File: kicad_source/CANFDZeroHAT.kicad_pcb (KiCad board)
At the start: 2 copper layers, 65 x 30 mm, 33 parts, among them CN1 RASPI-IO, CN2 691322310004, CN3 GH_SM04B-GHS-TB, CN4 GH_SM04B-GHS-TB, SW1 JS202011JCQN, U1 MCP2518FD, U2 TCAN332GDR, Y1 RH100-40.000-18-F-2050-TR

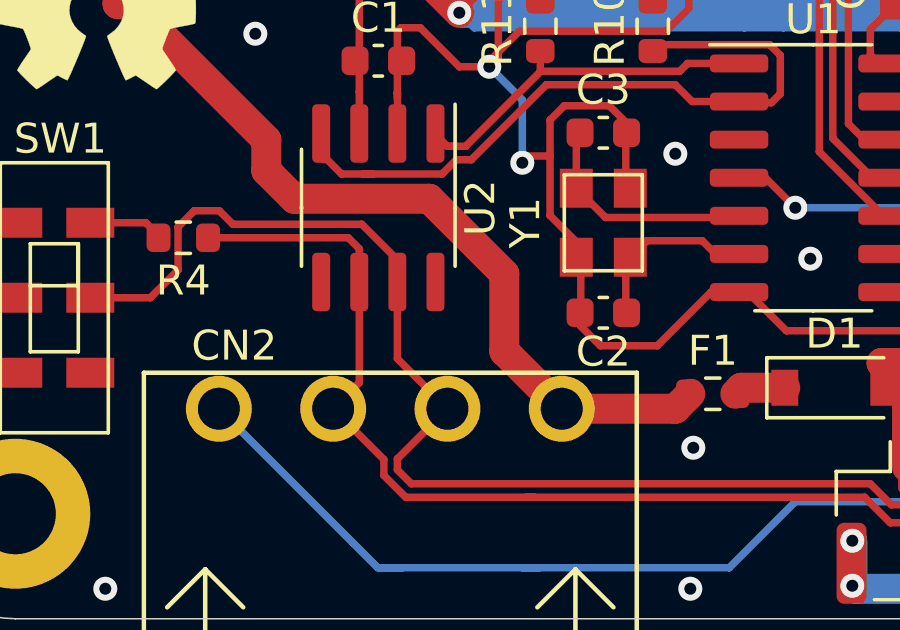
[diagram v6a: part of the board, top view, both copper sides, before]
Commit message: updated symbol of CAN driver
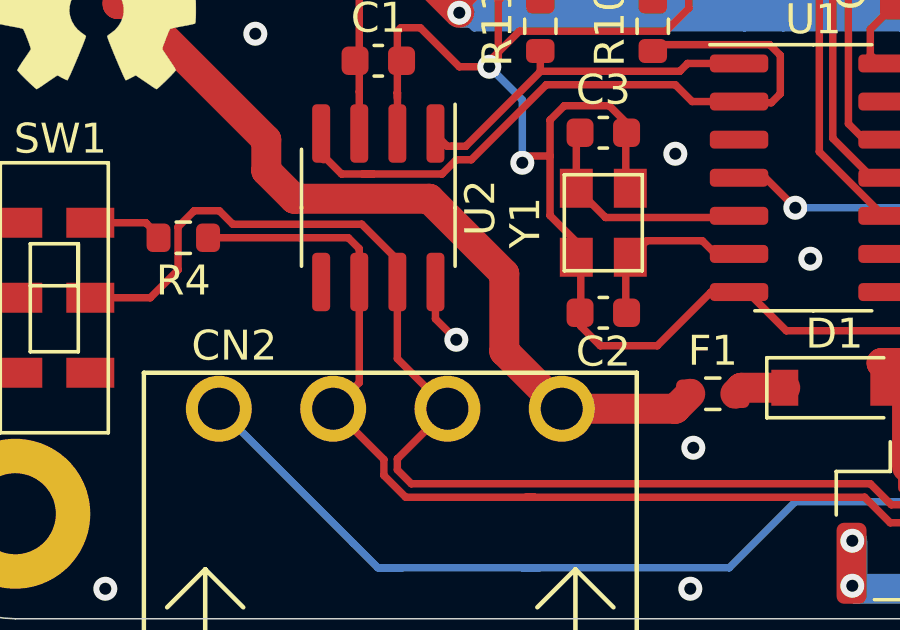
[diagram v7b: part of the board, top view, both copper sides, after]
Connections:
- U2 pad 8: unconnected-(U2-Pad8) -> GND
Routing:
- net GND: track 195.9 -> 198.1 mm, vias 22 -> 23
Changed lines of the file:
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@@
   (net 49 "unconnected-(U1-Pad9)")
   (net 50 "unconnected-(U2-Pad5)")
-  (net 51 "unconnected-(U2-Pad8)")
-  (net 52 "/MP")
-  (net 53 "unconnected-(SW1-Pad4)")
-  (net 54 "unconnected-(SW1-Pad5)")
-  (net 55 "unconnected-(SW1-Pad6)")
+  (net 51 "/MP")
+  (net 52 "unconnected-(SW1-Pad4)")
+  (net 53 "unconnected-(SW1-Pad5)")
+  (net 54 "unconnected-(SW1-Pad6)")
   (footprint "Capacitor_SMD:C_0603_1608Metric" (layer "F.Cu")
     (at 123.1 97.9)
@@
       (net 3 "GND") (pinfunction "Pin_4") (pintype "passive"))
     (pad "MP" smd roundrect (at 3.725 1.35) (size 1 2.7) (layers "F.Cu" "F.Paste" "F.Mask") (roundrect_rratio 0.25)
-      (net 52 "/MP") (pinfunction "MountPin") (pintype "passive"))
+      (net 51 "/MP") (pinfunction "MountPin") (pintype "passive"))
     (pad "MP" smd roundrect (at -3.725 1.35) (size 1 2.7) (layers "F.Cu" "F.Paste" "F.Mask") (roundrect_rratio 0.25)
-      (net 52 "/MP") (pinfunction "MountPin") (pintype "passive"))
+      (net 51 "/MP") (pinfunction "MountPin") (pintype "passive"))
     (model "${KICAD6_3DMODEL_DIR}/Connector_JST.3dshapes/JST_GH_SM04B-GHS-TB_1x04-1MP_P1.25mm_Horizontal.wrl"
       (offset (xyz 0 0 0))
@@
       (net 3 "GND") (pinfunction "Pin_4") (pintype "passive"))
     (pad "MP" smd roundrect (at 3.725 1.35) (size 1 2.7) (layers "F.Cu" "F.Paste" "F.Mask") (roundrect_rratio 0.25)
-      (net 52 "/MP") (pinfunction "MountPin") (pintype "passive"))
+      (net 51 "/MP") (pinfunction "MountPin") (pintype "passive"))
     (pad "MP" smd roundrect (at -3.725 1.35) (size 1 2.7) (layers "F.Cu" "F.Paste" "F.Mask") (roundrect_rratio 0.25)
-      (net 52 "/MP") (pinfunction "MountPin") (pintype "passive"))
+      (net 51 "/MP") (pinfunction "MountPin") (pintype "passive"))
     (model "${KICAD6_3DMODEL_DIR}/Connector_JST.3dshapes/JST_GH_SM04B-GHS-TB_1x04-1MP_P1.25mm_Horizontal.wrl"
       (offset (xyz 0 0 0))
@@
       (net 46 "unconnected-(SW1-Pad3)") (pinfunction "C") (pintype "passive+no_connect"))
     (pad "4" smd rect locked (at -2.5 1.2 270) (size 1 1.6) (layers "F.Cu" "F.Paste" "F.Mask")
-      (net 53 "unconnected-(SW1-Pad4)") (pinfunction "A") (pintype "passive+no_connect"))
+      (net 52 "unconnected-(SW1-Pad4)") (pinfunction "A") (pintype "passive+no_connect"))
     (pad "5" smd rect locked (at 0 1.2 270) (size 1 1.6) (layers "F.Cu" "F.Paste" "F.Mask")
-      (net 54 "unconnected-(SW1-Pad5)") (pinfunction "B") (pintype "passive+no_connect"))
+      (net 53 "unconnected-(SW1-Pad5)") (pinfunction "B") (pintype "passive+no_connect"))
     (pad "6" smd rect locked (at 2.5 1.2 270) (size 1 1.6) (layers "F.Cu" "F.Paste" "F.Mask")
-      (net 55 "unconnected-(SW1-Pad6)") (pinfunction "C") (pintype "passive+no_connect"))
+      (net 54 "unconnected-(SW1-Pad6)") (pinfunction "C") (pintype "passive+no_connect"))
     (model "${KISYS3DMOD}/mechanical-switches.3dshapes/JS202011JCQN.stp"
       (offset (xyz 0 0 0))
@@
     (fp_line (start -1.95 -1.475) (end -0.975 -2.45) (layer "F.Fab") (width 0.1))
     (pad "1" smd roundrect (at -2.475 -1.905 270) (size 1.95 0.6) (layers "F.Cu" "F.Paste" "F.Mask") (roundrect_rratio 0.25)
-      (net 17 "/CAN_TX") (pinfunction "D") (pintype "output"))
+      (net 17 "/CAN_TX") (pinfunction "D") (pintype "input"))
     (pad "2" smd roundrect (at -2.475 -0.635 270) (size 1.95 0.6) (layers "F.Cu" "F.Paste" "F.Mask") (roundrect_rratio 0.25)
       (net 3 "GND") (pinfunction "GND") (pintype "power_in"))
@@
       (net 1 "+3.3V") (pinfunction "VCC") (pintype "power_in"))
     (pad "4" smd roundrect (at -2.475 1.905 270) (size 1.95 0.6) (layers "F.Cu" "F.Paste" "F.Mask") (roundrect_rratio 0.25)
-      (net 18 "/CAN_RX") (pinfunction "R") (pintype "input"))
+      (net 18 "/CAN_RX") (pinfunction "R") (pintype "output"))
     (pad "5" smd roundrect (at 2.475 1.905 270) (size 1.95 0.6) (layers "F.Cu" "F.Paste" "F.Mask") (roundrect_rratio 0.25)
-      (net 50 "unconnected-(U2-Pad5)") (pinfunction "NC2") (pintype "bidirectional+no_connect"))
+      (net 50 "unconnected-(U2-Pad5)") (pinfunction "Vref") (pintype "output+no_connect"))
     (pad "6" smd roundrect (at 2.475 0.635 270) (size 1.95 0.6) (layers "F.Cu" "F.Paste" "F.Mask") (roundrect_rratio 0.25)
       (net 13 "/CANL") (pinfunction "CANL") (pintype "bidirectional"))
@@
       (net 12 "/CANH") (pinfunction "CANH") (pintype "bidirectional"))
     (pad "8" smd roundrect (at 2.475 -1.905 270) (size 1.95 0.6) (layers "F.Cu" "F.Paste" "F.Mask") (roundrect_rratio 0.25)
-      (net 51 "unconnected-(U2-Pad8)") (pinfunction "NC1") (pintype "bidirectional+no_connect"))
+      (net 3 "GND") (pinfunction "Rs") (pintype "input"))
     (model "${KICAD6_3DMODEL_DIR}/Package_SO.3dshapes/SOIC-8_3.9x4.9mm_P1.27mm.wrl"
       (offset (xyz 0 0 0))
@@
   (segment (start 126.03 92.53) (end 126.163262 92.53) (width 0.25) (layer "F.Cu") (net 3))
   (segment (start 122.037001 89.817001) (end 124.577001 89.817001) (width 0.25) (layer "F.Cu") (net 3))
+  (segment (start 125.005 106.505) (end 125.7 107.2) (width 0.25) (layer "F.Cu") (net 3))
   (segment (start 127.1 97.8) (end 126.8 98.1) (width 0.25) (layer "F.Cu") (net 3))
   (segment (start 140.3 94.55) (end 141.55 94.55) (width 0.25) (layer "F.Cu") (net 3))
@@
   (segment (start 130.5 107.4) (end 132.4 107.4) (width 0.25) (layer "F.Cu") (net 3))
   (segment (start 123.7385 100.0955) (end 123.7385 98.9685) (width 0.25) (layer "F.Cu") (net 3))
+  (segment (start 125.005 105.275) (end 125.005 106.505) (width 0.25) (layer "F.Cu") (net 3))
   (segment (start 127.1 95.9) (end 127.1 97.8) (width 0.25) (layer "F.Cu") (net 3))
   (segment (start 151.35 106.9) (end 152.1 106.9) (width 0.25) (layer "F.Cu") (net 3))
@@
   (via (at 114 87.5) (size 0.8) (drill 0.4) (layers "F.Cu" "B.Cu") (net 3))
   (via (at 127.9 101.3) (size 0.8) (drill 0.4) (layers "F.Cu" "B.Cu") (net 3))
+  (via (at 125.7 107.2) (size 0.8) (drill 0.4) (layers "F.Cu" "B.Cu") (net 3))
   (via (at 171.5 93.5) (size 0.8) (drill 0.4) (layers "F.Cu" "B.Cu") (net 3))
   (via (at 144.6 114.4) (size 0.8) (drill 0.4) (layers "F.Cu" "B.Cu") (net 3))
@@
   (segment (start 128.5 94.7507) (end 128.2493 94.5) (width 0.25) (layer "F.Cu") (net 26))
   (segment (start 128.5 96) (end 128.5 94.7507) (width 0.25) (layer "F.Cu") (net 26))
-  (via (at 156.8 115.4) (size 0.8) (drill 0.4) (layers "F.Cu" "B.Cu") (net 52))
-  (via (at 146.3 115.4) (size 0.8) (drill 0.4) (layers "F.Cu" "B.Cu") (net 52))
-  (via (at 149.4 115.4) (size 0.8) (drill 0.4) (layers "F.Cu" "B.Cu") (net 52))
-  (via (at 146.3 113.9) (size 0.8) (drill 0.4) (layers "F.Cu" "B.Cu") (net 52))
-  (via (at 156.8 113.9) (size 0.8) (drill 0.4) (layers "F.Cu" "B.Cu") (net 52))
-  (via (at 149.4 113.9) (size 0.8) (drill 0.4) (layers "F.Cu" "B.Cu") (net 52))
-  (via (at 138.9 115.4) (size 0.8) (drill 0.4) (layers "F.Cu" "B.Cu") (net 52))
-  (via (at 138.9 113.9) (size 0.8) (drill 0.4) (layers "F.Cu" "B.Cu") (net 52))
-  (segment (start 138.9 115.4) (end 139 115.5) (width 1) (layer "B.Cu") (net 52))
-  (segment (start 146.3 113.9) (end 146.3 115.4) (width 1) (layer "B.Cu") (net 52))
-  (segment (start 146.3 115.4) (end 149.4 115.4) (width 1) (layer "B.Cu") (net 52))
-  (segment (start 149.4 113.9) (end 149.4 115.4) (width 1) (layer "B.Cu") (net 52))
-  (segment (start 156.8 113.9) (end 156.8 115.4) (width 1) (layer "B.Cu") (net 52))
-  (segment (start 146.2 115.5) (end 146.3 115.4) (width 1) (layer "B.Cu") (net 52))
-  (segment (start 138.9 113.9) (end 138.9 115.4) (width 1) (layer "B.Cu") (net 52))
-  (segment (start 156.725 115.475) (end 156.8 115.4) (width 1) (layer "B.Cu") (net 52))
-  (segment (start 149.4 115.4) (end 149.475 115.475) (width 1) (layer "B.Cu") (net 52))
-  (segment (start 149.475 115.475) (end 156.725 115.475) (width 1) (layer "B.Cu") (net 52))
-  (segment (start 139 115.5) (end 146.2 115.5) (width 1) (layer "B.Cu") (net 52))
+  (via (at 156.8 115.4) (size 0.8) (drill 0.4) (layers "F.Cu" "B.Cu") (net 51))
+  (via (at 146.3 115.4) (size 0.8) (drill 0.4) (layers "F.Cu" "B.Cu") (net 51))
+  (via (at 149.4 115.4) (size 0.8) (drill 0.4) (layers "F.Cu" "B.Cu") (net 51))
+  (via (at 146.3 113.9) (size 0.8) (drill 0.4) (layers "F.Cu" "B.Cu") (net 51))
+  (via (at 156.8 113.9) (size 0.8) (drill 0.4) (layers "F.Cu" "B.Cu") (net 51))
+  (via (at 149.4 113.9) (size 0.8) (drill 0.4) (layers "F.Cu" "B.Cu") (net 51))
+  (via (at 138.9 115.4) (size 0.8) (drill 0.4) (layers "F.Cu" "B.Cu") (net 51))
+  (via (at 138.9 113.9) (size 0.8) (drill 0.4) (layers "F.Cu" "B.Cu") (net 51))
+  (segment (start 138.9 115.4) (end 139 115.5) (width 1) (layer "B.Cu") (net 51))
+  (segment (start 146.3 113.9) (end 146.3 115.4) (width 1) (layer "B.Cu") (net 51))
+  (segment (start 146.3 115.4) (end 149.4 115.4) (width 1) (layer "B.Cu") (net 51))
+  (segment (start 149.4 113.9) (end 149.4 115.4) (width 1) (layer "B.Cu") (net 51))
+  (segment (start 156.8 113.9) (end 156.8 115.4) (width 1) (layer "B.Cu") (net 51))
+  (segment (start 146.2 115.5) (end 146.3 115.4) (width 1) (layer "B.Cu") (net 51))
+  (segment (start 138.9 113.9) (end 138.9 115.4) (width 1) (layer "B.Cu") (net 51))
+  (segment (start 156.725 115.475) (end 156.8 115.4) (width 1) (layer "B.Cu") (net 51))
+  (segment (start 149.4 115.4) (end 149.475 115.475) (width 1) (layer "B.Cu") (net 51))
+  (segment (start 149.475 115.475) (end 156.725 115.475) (width 1) (layer "B.Cu") (net 51))
+  (segment (start 139 115.5) (end 146.2 115.5) (width 1) (layer "B.Cu") (net 51))
   (zone (net 3) (net_name "GND") (layer "F.Cu") (hatch edge 0.508)
     (connect_pads (clearance 0.508))

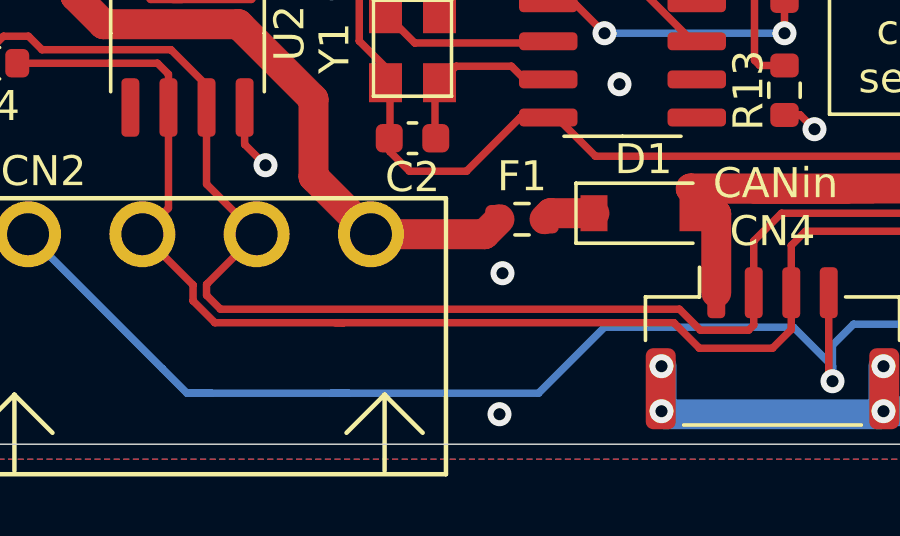
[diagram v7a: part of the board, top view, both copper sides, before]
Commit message: added protection on CAN, updated schematic pdf
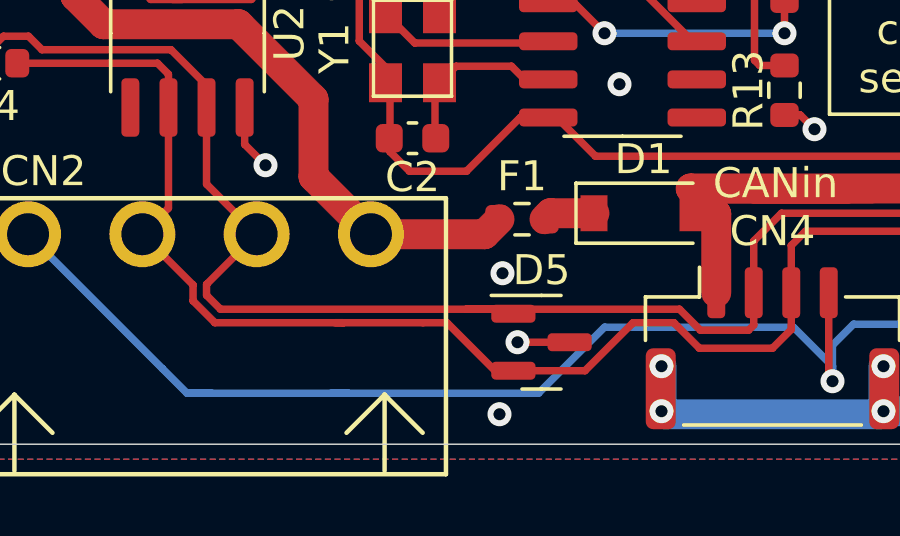
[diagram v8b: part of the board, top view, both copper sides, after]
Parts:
- added D5: DNI, Package_TO_SOT_SMD:SOT-23, F.Cu at (134.9, 113.1)
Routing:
- net GND: track 198.1 -> 199.8 mm, vias 23 -> 24
- net /CANH: track 56.5 -> 58.1 mm
- net /CANL: track 50.9 -> 52.3 mm
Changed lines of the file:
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@@
       ) (layer "F.SilkS") (width 0.01) (fill solid))
+  )
+  (footprint "Package_TO_SOT_SMD:SOT-23" (layer "F.Cu")
+    (at 134.9 113.1)
+    (descr "SOT, 3 Pin (https://www.jedec.org/system/files/docs/to-236h.pdf variant AB), generated with kicad-footprint-generator ipc_gullwing_generator.py")
+    (tags "SOT TO_SOT_SMD")
+    (property "Sheetfile" "CANFDZeroHAT.kicad_sch")
+    (property "Sheetname" "")
+    (attr smd)
+    (fp_text reference "D5" (at 0 -2.4) (layer "F.SilkS")
+      (effects (font (size 1 1) (thickness 0.15)))
+    )
+    (fp_text value "DNI" (at 0 2.4) (layer "F.Fab")
+      (effects (font (size 1 1) (thickness 0.15)))
+    )
+    (fp_text user "${REFERENCE}" (at 0 0) (layer "F.Fab")
+      (effects (font (size 0.32 0.32) (thickness 0.05)))
+    )
+    (fp_line (start 0 1.56) (end 0.65 1.56) (layer "F.SilkS") (width 0.12))
+    (fp_line (start 0 -1.56) (end 0.65 -1.56) (layer "F.SilkS") (width 0.12))
+    (fp_line (start 0 -1.56) (end -1.675 -1.56) (layer "F.SilkS") (width 0.12))
+    (fp_line (start 0 1.56) (end -0.65 1.56) (layer "F.SilkS") (width 0.12))
+    (fp_line (start -1.92 1.7) (end 1.92 1.7) (layer "F.CrtYd") (width 0.05))
+    (fp_line (start 1.92 1.7) (end 1.92 -1.7) (layer "F.CrtYd") (width 0.05))
+    (fp_line (start 1.92 -1.7) (end -1.92 -1.7) (layer "F.CrtYd") (width 0.05))
+    (fp_line (start -1.92 -1.7) (end -1.92 1.7) (layer "F.CrtYd") (width 0.05))
+    (fp_line (start 0.65 -1.45) (end 0.65 1.45) (layer "F.Fab") (width 0.1))
+    (fp_line (start -0.65 1.45) (end -0.65 -1.125) (layer "F.Fab") (width 0.1))
+    (fp_line (start -0.65 -1.125) (end -0.325 -1.45) (layer "F.Fab") (width 0.1))
+    (fp_line (start -0.325 -1.45) (end 0.65 -1.45) (layer "F.Fab") (width 0.1))
+    (fp_line (start 0.65 1.45) (end -0.65 1.45) (layer "F.Fab") (width 0.1))
+    (pad "1" smd roundrect (at -0.9375 -0.95) (size 1.475 0.6) (layers "F.Cu" "F.Paste" "F.Mask") (roundrect_rratio 0.25)
+      (net 12 "/CANH") (pinfunction "K") (pintype "passive"))
+    (pad "2" smd roundrect (at -0.9375 0.95) (size 1.475 0.6) (layers "F.Cu" "F.Paste" "F.Mask") (roundrect_rratio 0.25)
+      (net 13 "/CANL") (pinfunction "K") (pintype "passive"))
+    (pad "3" smd roundrect (at 0.9375 0) (size 1.475 0.6) (layers "F.Cu" "F.Paste" "F.Mask") (roundrect_rratio 0.25)
+      (net 3 "GND") (pinfunction "A") (pintype "passive"))
+    (model "${KICAD6_3DMODEL_DIR}/Package_TO_SOT_SMD.3dshapes/SOT-23.wrl"
+      (offset (xyz 0 0 0))
+      (scale (xyz 1 1 1))
+      (rotate (xyz 0 0 0))
+    )
   )
   (footprint "Resistor_SMD:R_0603_1608Metric" (layer "F.Cu")
@@
   (segment (start 143 105.525) (end 143.525 105.525) (width 0.25) (layer "F.Cu") (net 3))
   (segment (start 138.73 88.73) (end 139.817001 87.642999) (width 0.25) (layer "F.Cu") (net 3))
+  (segment (start 135.8375 113.1) (end 134.1 113.1) (width 0.25) (layer "F.Cu") (net 3))
   (segment (start 129.85 106.3) (end 129.85 104.6) (width 0.25) (layer "F.Cu") (net 3))
   (segment (start 138.73 88.73) (end 137.56 89.9) (width 0.25) (layer "F.Cu") (net 3))
@@
   (via (at 137.5 104.5) (size 0.8) (drill 0.4) (layers "F.Cu" "B.Cu") (net 3))
   (via (at 133 101) (size 0.8) (drill 0.4) (layers "F.Cu" "B.Cu") (net 3))
+  (via (at 134.1 113.1) (size 0.8) (drill 0.4) (layers "F.Cu" "B.Cu") (net 3))
   (via (at 133.6 110.8) (size 0.8) (drill 0.4) (layers "F.Cu" "B.Cu") (net 3))
   (via (at 114 115.5) (size 0.8) (drill 0.4) (layers "F.Cu" "B.Cu") (net 3))
@@
   (segment (start 123.735 111.535) (end 123.735 111.17) (width 0.25) (layer "F.Cu") (net 12))
   (segment (start 116.425001 104.874999) (end 116.425001 103.439997) (width 0.25) (layer "F.Cu") (net 12))
-  (segment (start 139.5 112) (end 124.2 112) (width 0.25) (layer "F.Cu") (net 12))
   (segment (start 117.8 102.9) (end 118.24999 103.34999) (width 0.25) (layer "F.Cu") (net 12))
   (segment (start 152.475 112.425) (end 152.475 111.45) (width 0.25) (layer "F.Cu") (net 12))
+  (segment (start 133.8125 112) (end 133.9625 112.15) (width 0.25) (layer "F.Cu") (net 12))
   (segment (start 142.9 108.8) (end 147.053232 108.8) (width 0.25) (layer "F.Cu") (net 12))
   (segment (start 141.975 111.45) (end 141.975 112.525) (width 0.25) (layer "F.Cu") (net 12))
@@
   (segment (start 122.54999 103.34999) (end 123.735 104.535) (width 0.25) (layer "F.Cu") (net 12))
   (segment (start 141.975 109.725) (end 142.9 108.8) (width 0.25) (layer "F.Cu") (net 12))
+  (segment (start 132.4 112) (end 133.8125 112) (width 0.25) (layer "F.Cu") (net 12))
+  (segment (start 132.4 112) (end 124.2 112) (width 0.25) (layer "F.Cu") (net 12))
   (segment (start 124.2 112) (end 123.735 111.535) (width 0.25) (layer "F.Cu") (net 12))
+  (segment (start 139.5 112) (end 132.4 112) (width 0.25) (layer "F.Cu") (net 12))
   (segment (start 118.24999 103.34999) (end 122.54999 103.34999) (width 0.25) (layer "F.Cu") (net 12))
   (segment (start 113.5 105.8) (end 115.5 105.8) (width 0.25) (layer "F.Cu") (net 12))
@@
   (segment (start 123.284991 111.721401) (end 123.28499 111.18999) (width 0.25) (layer "F.Cu") (net 13))
   (segment (start 153.63641 111.53859) (end 153.725 111.45) (width 0.25) (layer "F.Cu") (net 13))
+  (segment (start 133.9625 114.05) (end 133.35 114.05) (width 0.25) (layer "F.Cu") (net 13))
   (segment (start 123.28499 111.18999) (end 121.595 109.5) (width 0.25) (layer "F.Cu") (net 13))
   (segment (start 122.1 103.8) (end 120.5 103.8) (width 0.25) (layer "F.Cu") (net 13))
+  (segment (start 133.9625 114.05) (end 136.35 114.05) (width 0.25) (layer "F.Cu") (net 13))
+  (segment (start 131.75001 112.45001) (end 130.94999 112.45001) (width 0.25) (layer "F.Cu") (net 13))
   (segment (start 152.46139 113.07502) (end 153.63641 111.9) (width 0.25) (layer "F.Cu") (net 13))
   (segment (start 121.595 109.5) (end 122.465 108.63) (width 0.25) (layer "F.Cu") (net 13))
   (segment (start 124.0136 112.45001) (end 123.284991 111.721401) (width 0.25) (layer "F.Cu") (net 13))
   (segment (start 143.225 112.675) (end 143.225 111.45) (width 0.25) (layer "F.Cu") (net 13))
+  (segment (start 128.29999 112.45001) (end 130.94999 112.45001) (width 0.25) (layer "F.Cu") (net 13))
+  (segment (start 136.35 114.05) (end 137.94999 112.45001) (width 0.25) (layer "F.Cu") (net 13))
   (segment (start 122.465 108.63) (end 122.465 104.165) (width 0.25) (layer "F.Cu") (net 13))
-  (segment (start 128.29999 112.45001) (end 139.3136 112.45001) (width 0.25) (layer "F.Cu") (net 13))
   (segment (start 143.7 109.4) (end 147.016822 109.4) (width 0.25) (layer "F.Cu") (net 13))
   (segment (start 120.5 103.8) (end 117.35 103.8) (width 0.25) (layer "F.Cu") (net 13))
@@
   (segment (start 139.3136 112.45001) (end 140.16359 113.3) (width 0.25) (layer "F.Cu") (net 13))
   (segment (start 147.016822 109.4) (end 150.691842 113.07502) (width 0.25) (layer "F.Cu") (net 13))
+  (segment (start 138.34999 112.45001) (end 139.3136 112.45001) (width 0.25) (layer "F.Cu") (net 13))
   (segment (start 142.6 113.3) (end 143.225 112.675) (width 0.25) (layer "F.Cu") (net 13))
+  (segment (start 133.35 114.05) (end 131.75001 112.45001) (width 0.25) (layer "F.Cu") (net 13))
+  (segment (start 137.94999 112.45001) (end 138.34999 112.45001) (width 0.25) (layer "F.Cu") (net 13))
   (segment (start 151.225 111.45) (end 151.225 110.225) (width 1) (layer "F.Cu") (net 14))
   (segment (start 149.14999 108.34999) (end 151.225 110.425) (width 0.25) (layer "F.Cu") (net 14))
